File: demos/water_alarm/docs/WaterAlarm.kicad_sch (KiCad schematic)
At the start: 6 parts, among them U2 SN74HC04, U3 CD4069

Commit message: export: kicad_sch — Phase 2.5b: layered placement, wire routing, KiCad 10 compatibility (#23)
* export: kicad_sch — Phase 2.5b: layered placement + routing + KiCad 9 fix

Placement (placement.py, complete rewrite):
- Replaces naive grid with Layered Signal Flow algorithm (spec §5 stages 1–8)
- Stage 1: band classification — power chips/rails at top, LEDs at bottom,
  everything else in the signal band
- Stage 2: signal-flow DAG via BFS from Rail/Connector sources; layer = BFS
  distance from nearest source
- Stage 3–4: place within (band, layer) cells at 1500-mil (38.1 mm) same-band
  spacing, 1000-mil inter-band gutter, 25.4 mm page margin
- Stage 6: cluster breakup — up to 10 iterations shifting same-band parts
  that land closer than 0.9× SAME_BAND_SPACING_MM
- Stage 8: page sized to fit (A4 → A3 → A2 → A1)
- grid_place() and sheet_size_mm() kept as shims for backward-compat

Routing (routing.py, new file):
- route_net(): connects stub ends with Manhattan L-shapes (horizontal first)
- find_junctions(): returns points where ≥3 wire endpoints coincide
- renderer uses routed wires between signal-net stub ends

Hierarchical (hierarchical.py, new file):
- collect_boards(), is_multi_board(), sub_sheet_filename() — interface stub
  for multi-Board sub-sheet emission (full implementation deferred)

KiCad 9 sub-symbol name fix (library_loader.py):
- KiCad 9 schematics expect sub-symbols nested inside their parent in
  lib_symbols to use the bare name (R_0_1, LED_0_1, 4069_1_0) — NOT the
  lib-qualified name (Device:R_0_1, Device:LED_0_1, 4xxx:4069_1_0)
- Fixed _qualify_names() to add the lib: prefix only to the exact parent
  symbol name using a lookahead (?=") that prevents sub-unit names from
  being qualified

Tests (+25 tests):
- test_placement.py: band classification, all-on-grid, determinism,
  minimum spacing, power < signal < indicator Y ordering, page sizing
- test_routing.py: H/V segments, L-shapes, orthogonality, grid snap,
  junction detection

Golden files re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
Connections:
- net Net-(D2-anode): now also D2.2 (A)
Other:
- moved on the sheet: D1, D2, R1, R2, U2A, U3A

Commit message: framework: LED.cathode mandatory + close WaterAlarm regression (#29)
Found while reviewing WaterAlarm's breadboard SVG: the LEDs in the
design had no ground connections drawn. Investigation revealed
`LED.cathode` was declared `mandatory=False` with the docstring claim
*"floating = GND"* — a "structurally inert under graph evaluation"
shortcut that lets demos write electrically-broken circuits and have
them pass ERC.

A real LED with a dangling cathode does not light. This is exactly
the kind of physical-fidelity violation `CLAUDE.md` lists as
disallowed.

  - `src/components/passives/led.py`: `cathode` becomes
    `mandatory=True`. Docstring updated to drop the "floating = GND"
    claim and explain the contract.
  - `tests/components/test_led.py`: regression tests pin both ports
    as mandatory and confirm `Circuit.__init__` raises
    `UnconnectedPinError` end-to-end when a cathode is left
    floating.
  - `demos/water_alarm/water_alarm.py` and
    `demos/water_alarm_split/water_alarm_split.py`: cathodes wired
    to the GND rail. (Bench builds still need a series current-limit
    resistor; the logic-level demo doesn't model V_F or current.)
  - `tests/framework/test_circuit_autocollect.py`,
    `tests/framework/test_framework.py`, and
    `tests/framework/import_kicad/test_import.py`: fixtures that
    leaned on the broken default updated so they still pin down the
    specific error each test exists to catch.
  - Demo docs regenerated for the two WaterAlarm variants.
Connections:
- net Net-(D2-anode) is gone; now on net GND: D2.1 (K), D2.2 (A), U3.2
- net GND: now also D1.2 (A)
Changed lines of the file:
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@@
+  )
+  (symbol
+    (lib_id "power:GND")
+    (at 69.85 1270 270)
+    (unit 1)
+    (exclude_from_sim no)
+    (in_bom yes)
+    (on_board yes)
+    (dnp no)
+    (property "Reference" "#PWR"
+      (at 69.85 1270 0)
+      (effects (font (size 1.27 1.27)) (hide yes))
+    )
+    (property "Value" "GND"
+      (at 69.85 1270 0)
+      (effects (font (size 1.27 1.27)))
+    )
+    (pin "1")
   )
   (symbol
@@
   )
   (symbol
+    (lib_id "power:GND")
+    (at 69.85 1308.1 270)
+    (unit 1)
+    (exclude_from_sim no)
+    (in_bom yes)
+    (on_board yes)
+    (dnp no)
+    (property "Reference" "#PWR"
+      (at 69.85 1308.1 0)
+      (effects (font (size 1.27 1.27)) (hide yes))
+    )
+    (property "Value" "GND"
+      (at 69.85 1308.1 0)
+      (effects (font (size 1.27 1.27)))
+    )
+    (pin "1")
+  )
+  (symbol

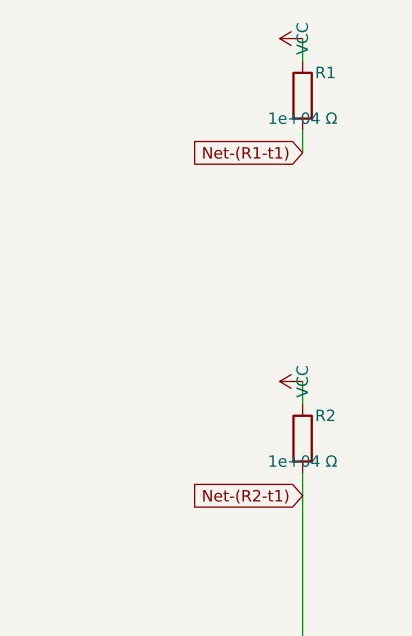
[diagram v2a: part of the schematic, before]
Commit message: units: Ohms.__str__ uses engineering notation (kΩ, MΩ, GΩ)
The previous `Ohms.__str__` formatted with bare `:.3g`, producing
unreadable scientific output for clean kilo / mega multiples:

  str(Ohms(10_000))     == "1e+04 Ω"      → now "10 kΩ"
  str(Ohms(100_000))    == "1e+05 Ω"      → now "100 kΩ"
  str(Ohms(1_000_000))  == "1e+06 Ω"      → now "1 MΩ"

The breadboard SVG visualiser surfaced the problem: a resistor body
labelled "100000Ω" makes a reader count zeros, while a label of
"100 kΩ" reads at a glance — exactly the convention every schematic
and parts catalogue uses. Centralising the engineering notation in
`Ohms.__str__` means every downstream consumer (assembly guide,
breadboard SVG, kicad netlist, BOM, reports) inherits the readable
form without each format adapter rolling its own formatter.

  - `Ohms.__str__` returns "47 Ω", "4.7 kΩ", "10 kΩ", "100 kΩ",
    "1 MΩ", "10 MΩ", "1 GΩ" per the kilo / mega / giga thresholds.
  - `Resistor.__str__` delegates to `str(self._ohms)` so it
    inherits the new notation (was producing the noisy "47.0 Ω"
    via raw float).
  - The breadboard visualiser's resistor body label uses
    `str(part.ohms)` directly (previously had a private
    `_format_ohms_compact` helper; removed).
  - `tests/components/test_resistor.py::test_str` updated for
    "47 Ω" (was "47.0 Ω"); new `test_str_renders_in_engineering_notation`
    pins kΩ / MΩ output across the kilo and mega thresholds.
  - All demo docs / goldens refreshed where the Ohms.__str__
    change affected the rendered output (breadboard SVGs, kicad
    sch value fields, BOM rows).
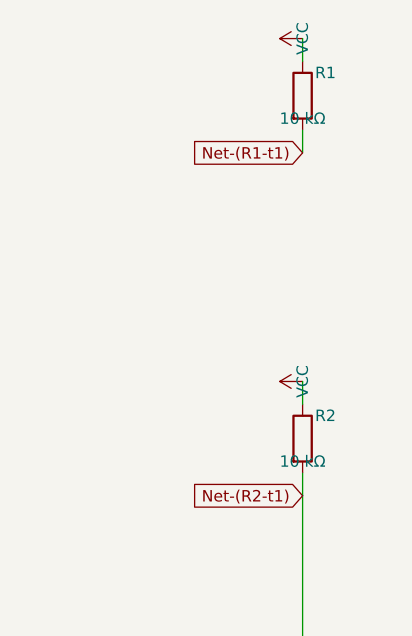
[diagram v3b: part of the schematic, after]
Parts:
- R1, R2: value 1e+04 Ω -> 10 kΩ
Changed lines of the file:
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@@
       (effects (font (size 1.27 1.27)))
     )
-    (property "Value" "1e+04 Ω"
+    (property "Value" "10 kΩ"
       (at 63.5 866.14 0)
       (effects (font (size 1.27 1.27)))
@@
       (effects (font (size 1.27 1.27)))
     )
-    (property "Value" "1e+04 Ω"
+    (property "Value" "10 kΩ"
       (at 63.5 904.24 0)
       (effects (font (size 1.27 1.27)))
